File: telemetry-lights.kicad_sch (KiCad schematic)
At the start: 25 parts, among them J1 Conn_01x02, J2 Conn_01x04, J6 Conn_01x02, J8 Conn_01x02, U1 STM32L431KBU6TR, U2 INA228, U3 IAM-20381HT

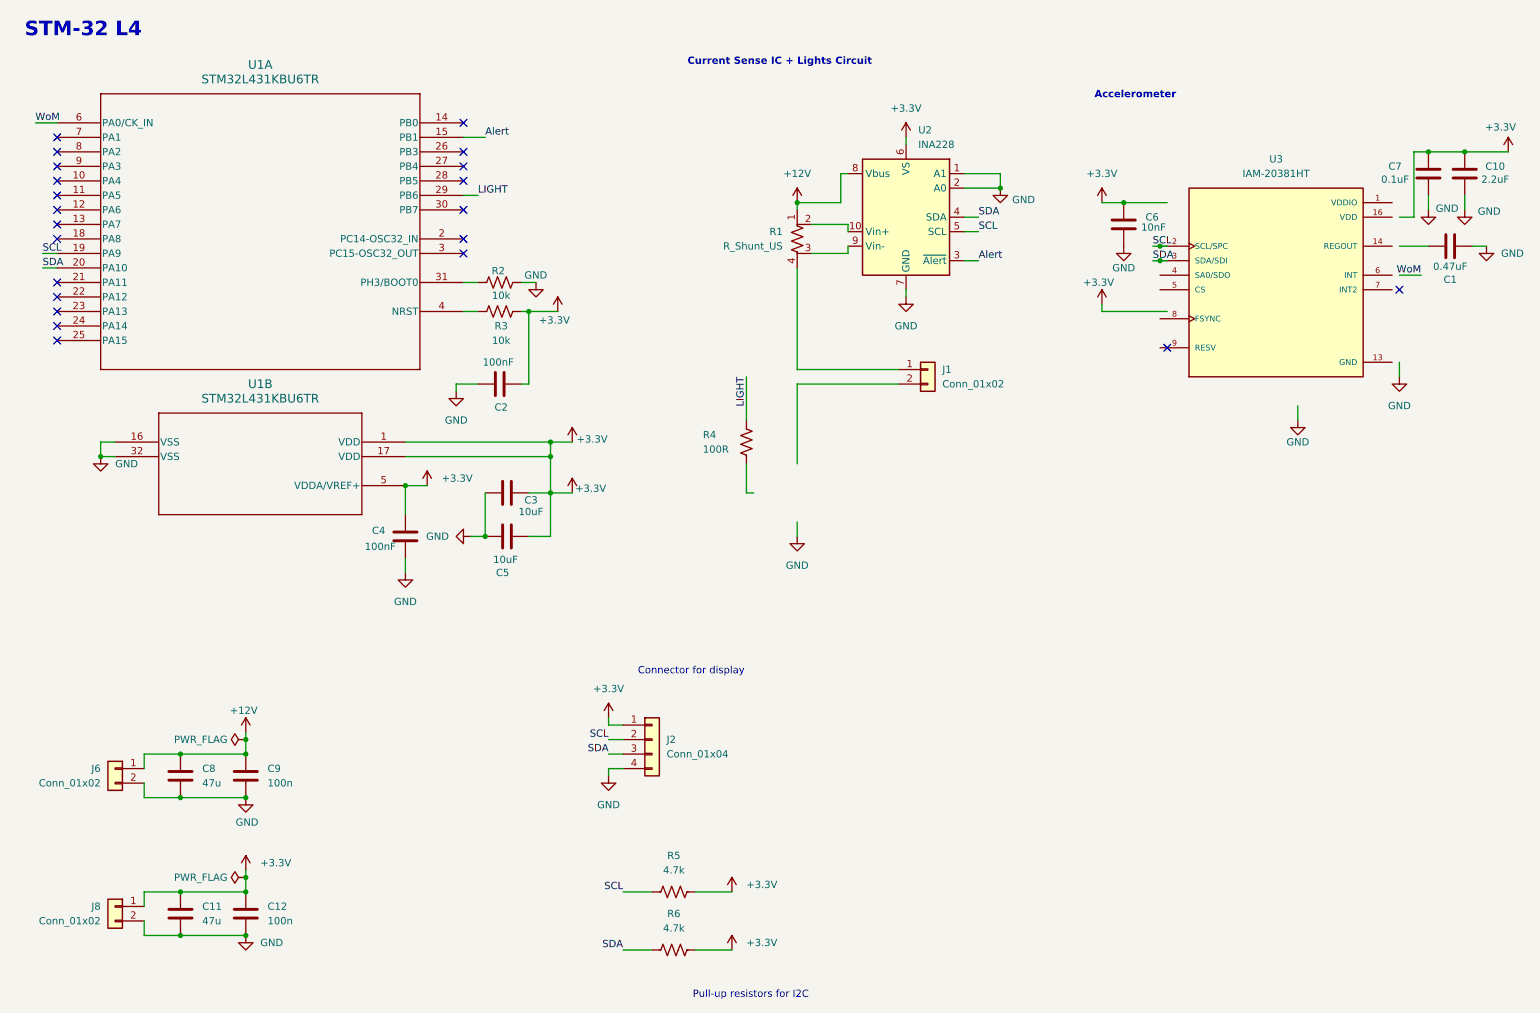
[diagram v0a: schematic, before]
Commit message: Added STM chip to all libraries + CAD, fixed up accelorometer in schematic (still not done)
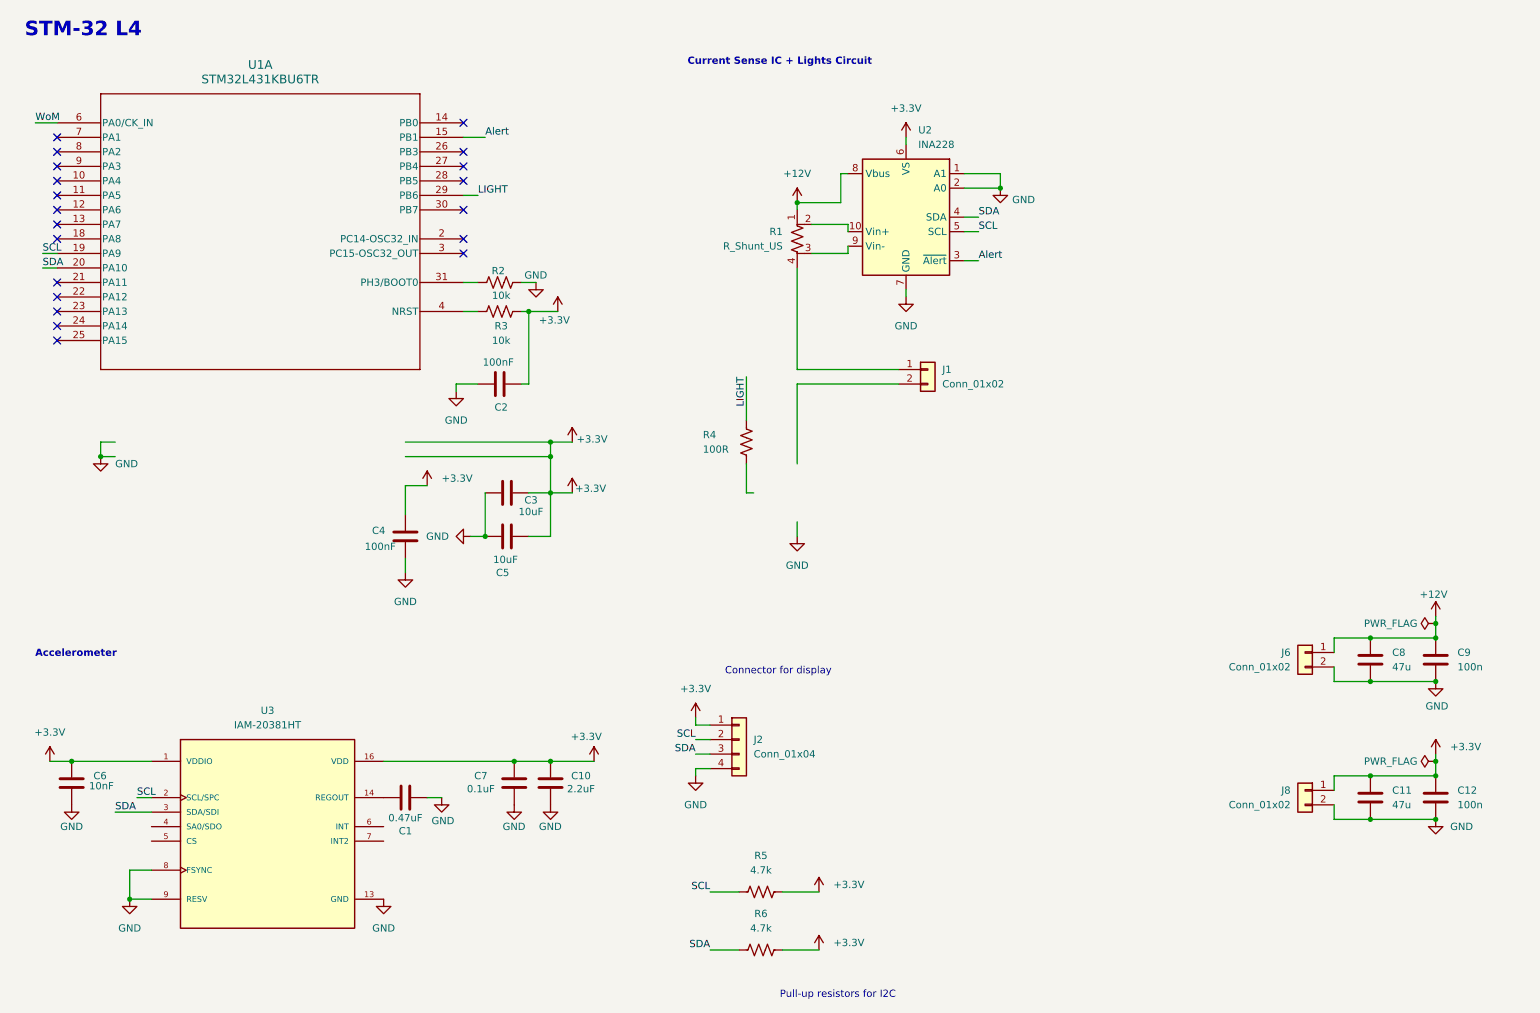
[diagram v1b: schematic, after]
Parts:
- removed U1: STM32L431KBU6TR, telemetry-lights:UFQFPN-32, symbol telemetry-lights:STM32L431KBU6TR
- added U1: STM32L431KBU6TR, skateboard-footprint-library:UFQFPN-32, symbol skateboard-symbol-library:STM32L431KBU6TR
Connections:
- net +3.3V: now also U3.1 (VDDIO), U3.16 (VDD)
- net Alert: now also U1.15 (PB1)
- net GND: now also U3.10 (RESV), U3.11 (RESV), U3.12 (RESV), U3.13 (GND), U3.15 (RESV), U3.8 (FSYNC), U3.9 (RESV)
- net LIGHT: now also U1.29 (PB6)
- net SCL: now also U1.19 (PA9)
- net SDA: now also U1.20 (PA10)
- net WoM: now also U1.6 (PA0/CK_IN)
- net at U3.14 (REGOUT): now also C1.2
- net at R2.1: now also U1.31 (PH3/BOOT0)
- net at R3.1: now also U1.4 (NRST)
- no-connect marks 22 -> 20
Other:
- moved on the sheet: C1, C10, C11, C12, C6, C7, C8, C9, J2, J6, J8, R5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

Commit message: Add test points and replace pull-up resistors
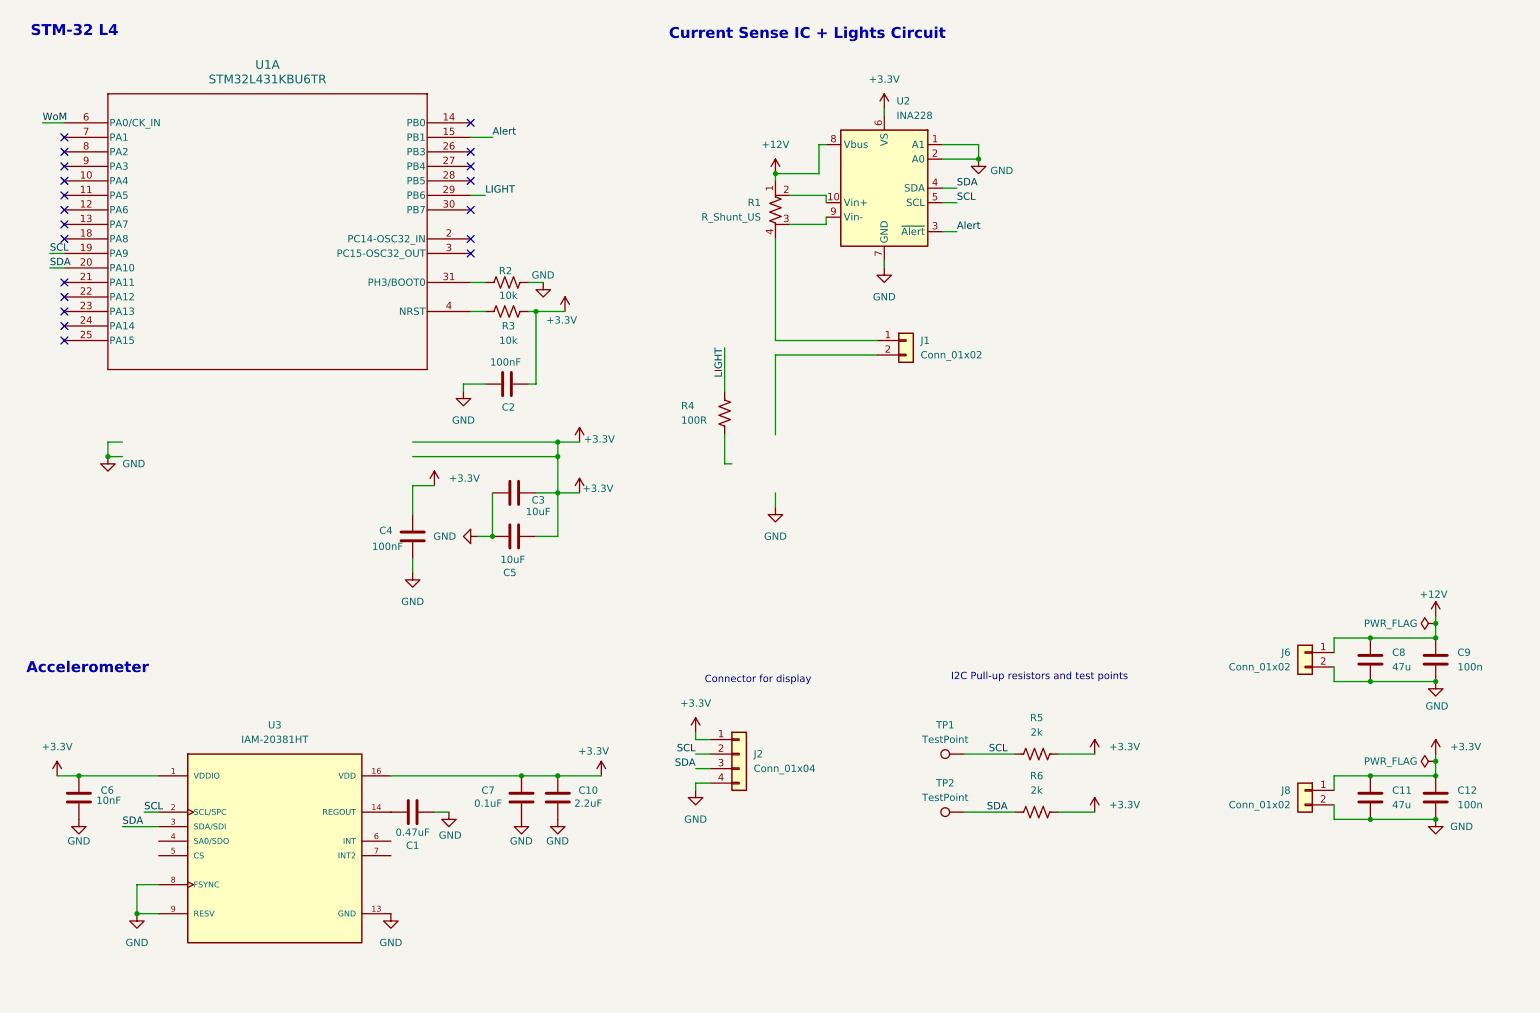
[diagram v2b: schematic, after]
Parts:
- added TP1, TP2: TestPoint, TestPoint:TestPoint_Pad_D1.0mm, symbol Connector:TestPoint
- R5, R6: value 4.7k -> 2k
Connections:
- net SCL: now also TP1.1
- net SDA: now also TP2.1
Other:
- note added: "I2C Pull-up resistors and test points"
- note removed: "Pull-up resistors for I2C"
- company: (none) -> Electrium Mobility
- title: (none) -> Skateboard
- moved on the sheet: C1, C10, C2, C3, C4, C5, C6, C7, J1, J2, R1, R2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

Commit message: Label interrupt pins and add no connect flags
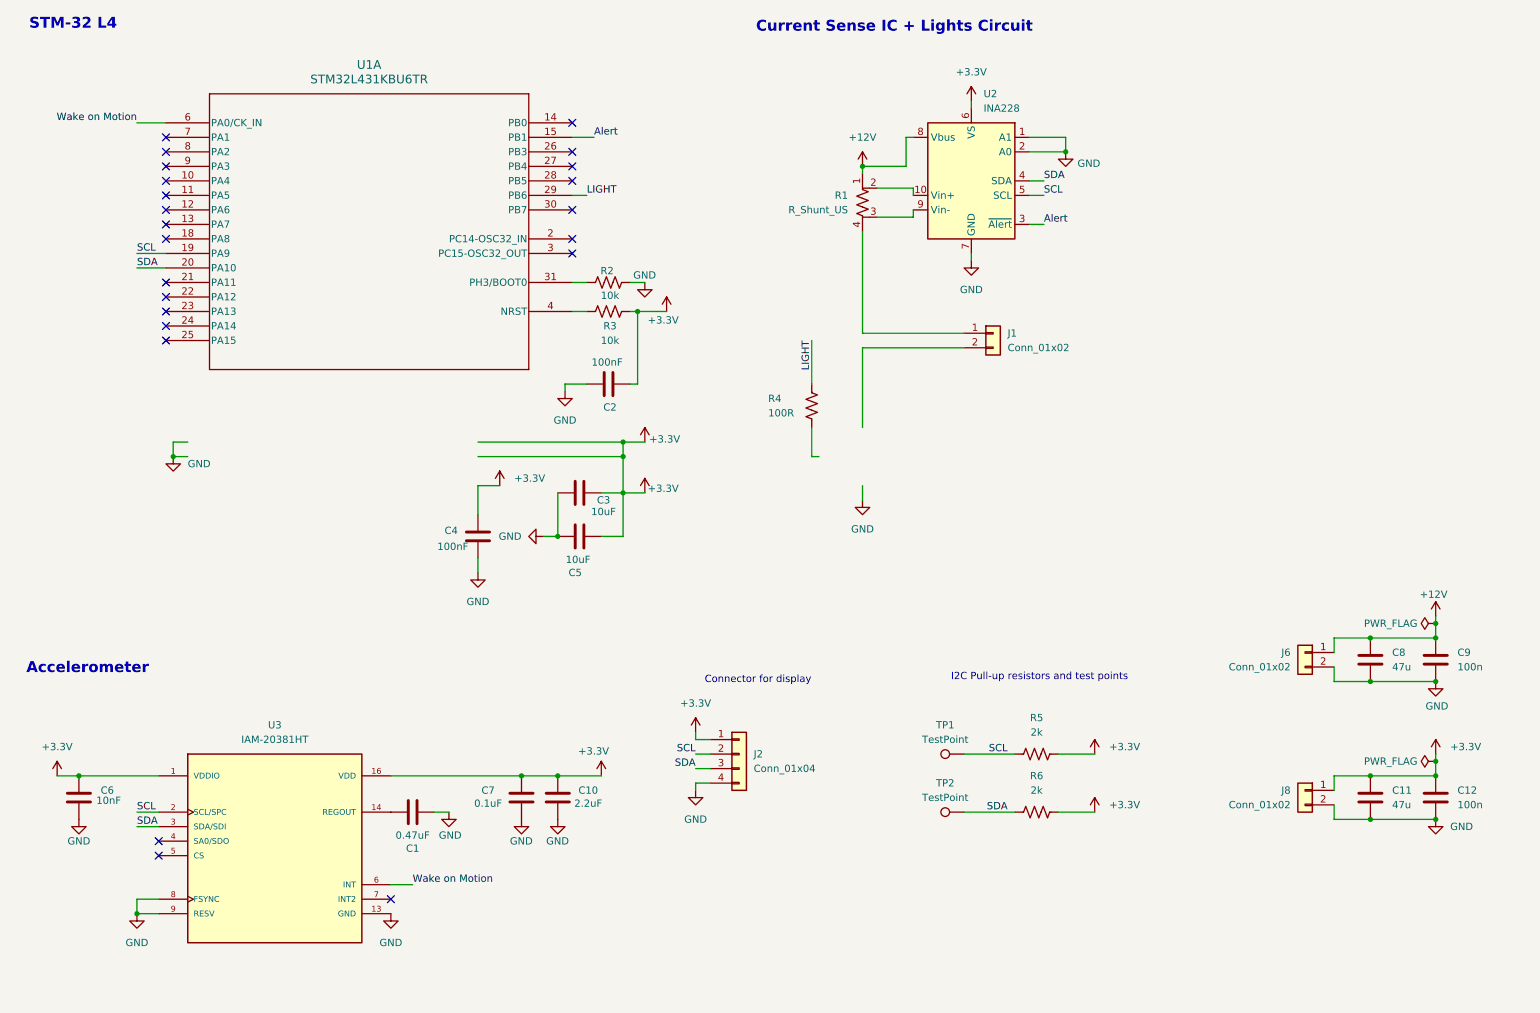
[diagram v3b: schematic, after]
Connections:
- net WoM is gone; now on net Wake on Motion: U1.6 (PA0/CK_IN)
- net Wake on Motion: now reaches U3.6 (INT)
- no-connect marks 20 -> 23
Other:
- moved on the sheet: C2, C3, C4, C5, J1, R1, R2, R3, R4, U1A, U2

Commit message: altered schematic
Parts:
- removed J1: Conn_01x02, Connector_JST:JST_PH_B2B-PH-K_1x02_P2.00mm_Vertical, symbol Connector_Generic:Conn_01x02
- removed R1: R_Shunt_US, Resistor_SMD:R_Shunt_Ohmite_LVK20, symbol Device:R_Shunt_US
- removed R4: 100R, Resistor_SMD:R_0805_2012Metric_Pad1.20x1.40mm_HandSolder, symbol Device:R_US
- removed U1: STM32L431KBU6TR, skateboard-footprint-library:UFQFPN-32, symbol skateboard-symbol-library:STM32L431KBU6TR
- removed U2: INA228, telemetry-lights:VSSOP-10_3x3mm_P0.5mm, symbol Sensor_Energy:INA228
- added J3: Conn_01x03, Connector_JST:JST_EH_B3B-EH-A_1x03_P2.50mm_Vertical, symbol Connector_Generic:Conn_01x03
- added U2: STM32L431KBU6TR, UFQFPN-32, symbol telemetry-lights:STM32L431KBU6TR
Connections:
- net +12V: now also J3.1 (Pin_1)
- net +3.3V: now also U2.1 (VDD), U2.17 (VDD), U2.5 (VDDA/VREF+)
- net Alert: now also U2.15 (PB1)
- net GND: now also J3.3 (Pin_3), U2.16 (VSS), U2.32 (VSS)
- net LIGHT: now also J3.2 (Pin_2), U2.29 (PB6)
- net SCL: now also U2.19 (PA9)
- net SDA: now also U2.20 (PA10)
- net Wake on Motion: now also U2.6 (PA0/CK_IN)
- net at R2.1: now also U2.31 (PH3/BOOT0)
- net at R3.1: now also U2.4 (NRST)
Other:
- note added: "Lights Circuit"
- note added: "Power Connectors"
- note removed: "Current Sense IC + Lights Circuit"

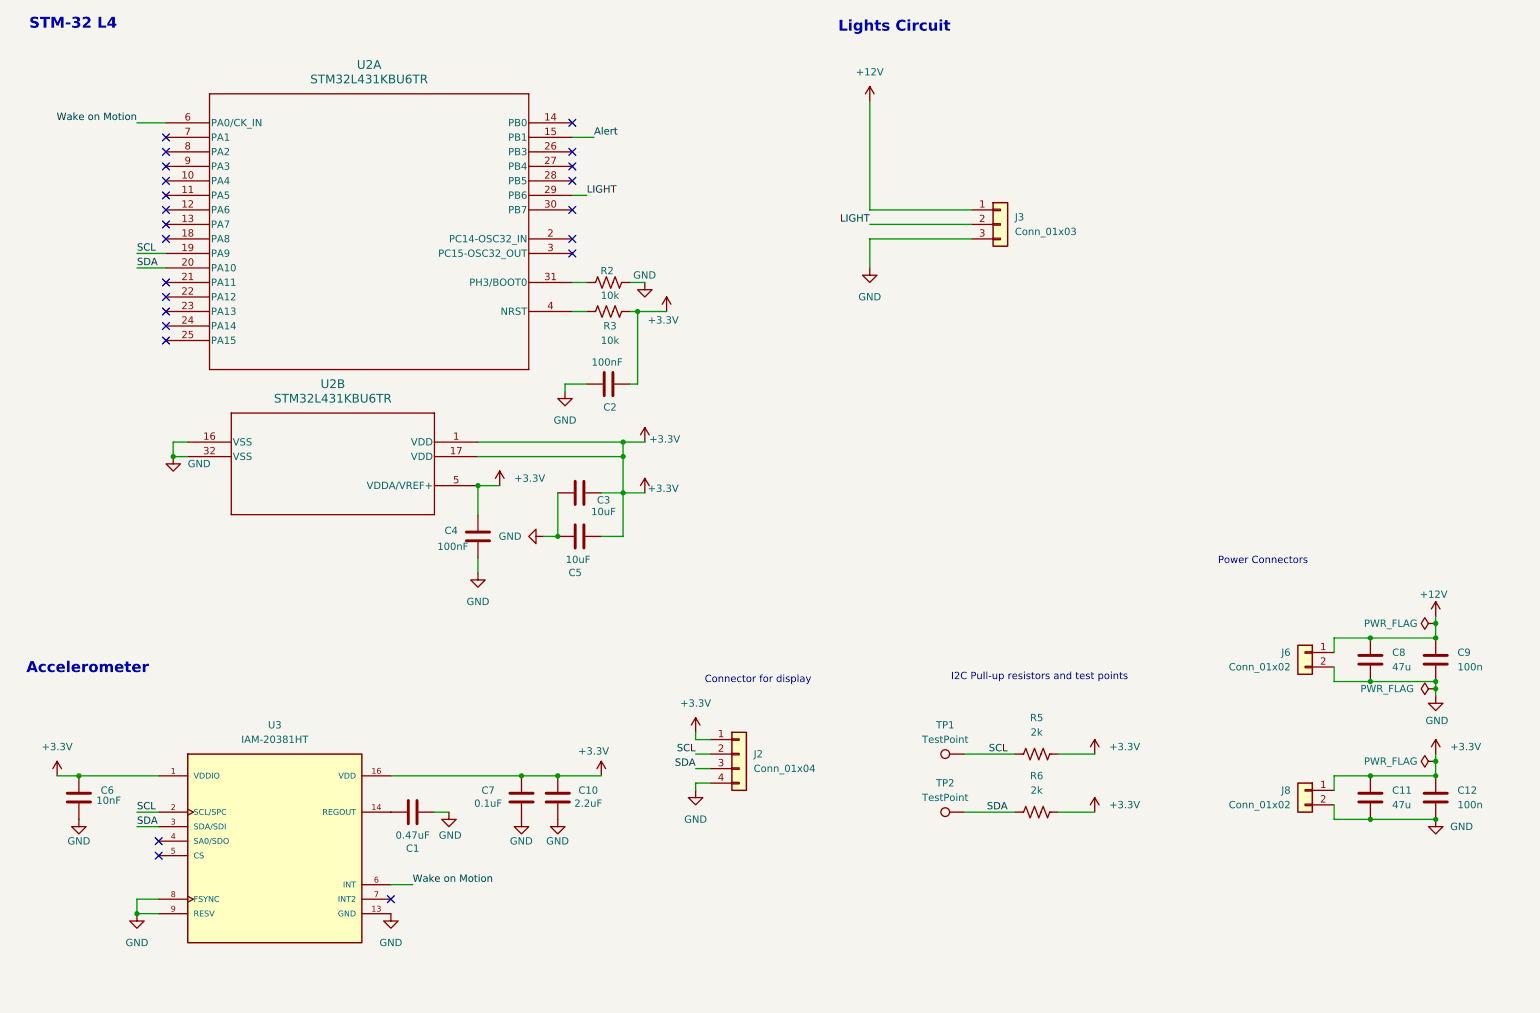
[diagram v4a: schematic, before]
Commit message: reorganized schematic
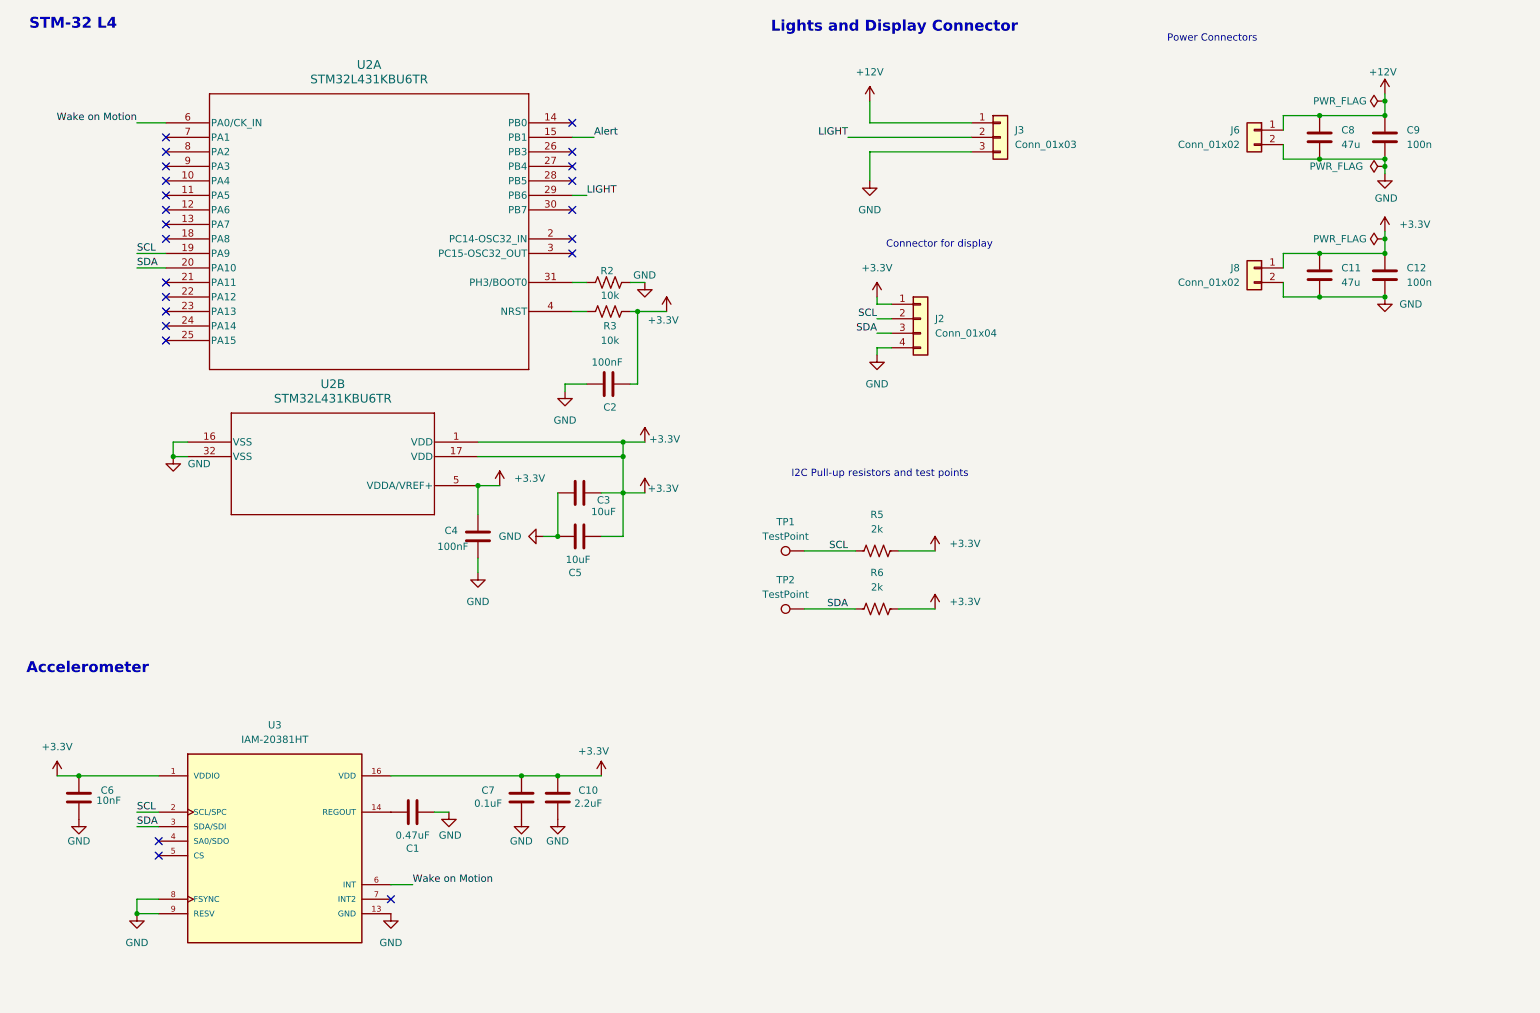
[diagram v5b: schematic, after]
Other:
- note added: "Lights and Display Connector"
- note removed: "Lights Circuit"
- moved on the sheet: C11, C12, C8, C9, J2, J3, J6, J8, R5, R6, TP1, TP2
